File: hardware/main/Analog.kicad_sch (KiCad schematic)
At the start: 61 parts, among them J301 Overvoltage_protection, J302 Rad_sensor, J303 Mos_temp, J304 Diode_temp, U301 INA823DT, U302 INA823DT, U303 INA293A4, U304 INA293A4, U305 TL7726IDR_1

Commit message: Layout: Organize and initialize routing of control
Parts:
- added C315: 50V 100nF 0805, Capacitor_SMD:C_0805_2012Metric_Pad1.18x1.45mm_HandSolder, symbol Device:C_Small
- added D308: ESD351DPYR, Diode_SMD:D_0402_1005Metric_Pad0.77x0.64mm_HandSolder, symbol Device:D_TVS
- added R326: ?, Resistor_SMD:R_0805_2012Metric_Pad1.20x1.40mm_HandSolder, symbol Device:R_Small
- added TH303: NTC 10k 1SDNT2012X103F3950FTF, Resistor_SMD:R_0805_2012Metric_Pad1.20x1.40mm_HandSolder, symbol Device:Thermistor_NTC
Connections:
- net 3V3: now also R326.2
- net GNDA: now also C315.2, D308.1 (A1), TH303.2
- net I_panel_adc+: no longer D306.2 (A2)
- net V_bat_adc+: now also D306.2 (A2)
- new net V_temp_amb: C315.1, D308.2 (A2), R326.1, TH303.1
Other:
- moved on the sheet: C302, C303, J303, J304, R301, R302, TH301, TH302

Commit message: Schematics: Switch 2 Clamp inputs for better routing
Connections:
- net V_panel_adc+: now also U305.6 (D5); no longer U305.2 (D1)
- net V_temp_diode: now also U305.2 (D1); no longer U305.6 (D5)
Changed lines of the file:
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@@
     (stroke (width 0) (type default) (color 0 0 0 0))
   )
-  (label "V_panel_adc+" (at 179.07 45.72 0)
+  (label "V_panel_adc+" (at 222.885 53.34 0)
     (effects (font (size 1.016 1.016)) (justify left bottom))
   )
@@
     (effects (font (size 1.016 1.016)) (justify left bottom))
   )
-  (label "V_temp_diode" (at 222.885 53.34 0)
+  (label "V_temp_diode" (at 179.07 45.72 0)
     (effects (font (size 1.016 1.016)) (justify left bottom))
   )

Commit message: Layout: Designing thermal dissipation and optimizing control
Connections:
- net V_bat_adc+: now also U305.2 (D1); no longer U305.3 (D2)
- net V_panel_adc+: now also U305.7 (D6); no longer U305.6 (D5)
- net V_temp_diode: now also U305.6 (D5); no longer U305.2 (D1)
- net V_temp_mos: now also U305.3 (D2); no longer U305.7 (D6)
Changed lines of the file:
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@@
     (stroke (width 0) (type default) (color 0 0 0 0))
   )
-  (label "V_panel_adc+" (at 222.885 53.34 0)
+  (label "V_panel_adc+" (at 223.52 60.96 0)
     (effects (font (size 1.016 1.016)) (justify left bottom))
   )
@@
     (effects (font (size 1.016 1.016)) (justify left bottom))
   )
-  (label "V_temp_diode" (at 179.07 45.72 0)
+  (label "V_temp_diode" (at 222.885 53.34 0)
     (effects (font (size 1.016 1.016)) (justify left bottom))
   )
@@
     (effects (font (size 1.016 1.016)) (justify left bottom))
   )
-  (label "V_temp_mos" (at 223.52 60.96 0)
+  (label "V_temp_mos" (at 179.07 53.34 0)
     (effects (font (size 1.016 1.016)) (justify left bottom))
   )
@@
     (effects (font (size 1.016 1.016)) (justify left bottom))
   )
-  (label "V_bat_adc+" (at 179.07 53.34 0)
+  (label "V_bat_adc+" (at 179.07 45.72 0)
     (effects (font (size 1.016 1.016)) (justify left bottom))
   )

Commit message: Layout: Connect all unconected nets, and fix all DRC errors
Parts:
- JP301, JP302, JP303, JP304: footprint Zenite:SolderJumper-2_P0.5mm_Open_TrianglePad0.5x0.5mm -> Zenite:SolderJumper-2_P0.5mm_Open_TrianglePad0.8x0.5mm
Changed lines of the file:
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@@
     (property "Reference" "JP304" (id 0) (at 257.175 53.4502 0))
     (property "Value" "Disable_Ibat" (id 1) (at 257.175 55.9871 0))
-    (property "Footprint" "Zenite:SolderJumper-2_P0.5mm_Open_TrianglePad0.5x0.5mm" (id 2) (at 257.175 57.785 0)
+    (property "Footprint" "Zenite:SolderJumper-2_P0.5mm_Open_TrianglePad0.8x0.5mm" (id 2) (at 257.175 57.785 0)
       (effects (font (size 1.27 1.27)) hide)
     )
@@
     (property "Reference" "JP301" (id 0) (at 257.175 36.3052 0))
     (property "Value" "Disable_Vpanel" (id 1) (at 257.175 38.8421 0))
-    (property "Footprint" "Zenite:SolderJumper-2_P0.5mm_Open_TrianglePad0.5x0.5mm" (id 2) (at 257.175 40.64 0)
+    (property "Footprint" "Zenite:SolderJumper-2_P0.5mm_Open_TrianglePad0.8x0.5mm" (id 2) (at 257.175 40.64 0)
       (effects (font (size 1.27 1.27)) hide)
     )
@@
     (property "Reference" "JP302" (id 0) (at 257.175 42.0202 0))
     (property "Value" "Disable_Vbat" (id 1) (at 257.175 44.5571 0))
-    (property "Footprint" "Zenite:SolderJumper-2_P0.5mm_Open_TrianglePad0.5x0.5mm" (id 2) (at 257.175 46.355 0)
+    (property "Footprint" "Zenite:SolderJumper-2_P0.5mm_Open_TrianglePad0.8x0.5mm" (id 2) (at 257.175 46.355 0)
       (effects (font (size 1.27 1.27)) hide)
     )
@@
     (property "Reference" "JP303" (id 0) (at 257.175 47.7352 0))
     (property "Value" "Disabel_Ipanel" (id 1) (at 257.175 50.2721 0))
-    (property "Footprint" "Zenite:SolderJumper-2_P0.5mm_Open_TrianglePad0.5x0.5mm" (id 2) (at 257.175 52.07 0)
-      (effects (font (size 1.27 1.27)) hide)
-    )
+    (property "Footprint" "Zenite:SolderJumper-2_P0.5mm_Open_TrianglePad0.8x0.5mm" (id 2) (at 257.175 52.07 0)
+      (effects (font (size 1.27 1.27)) hide)
+    )

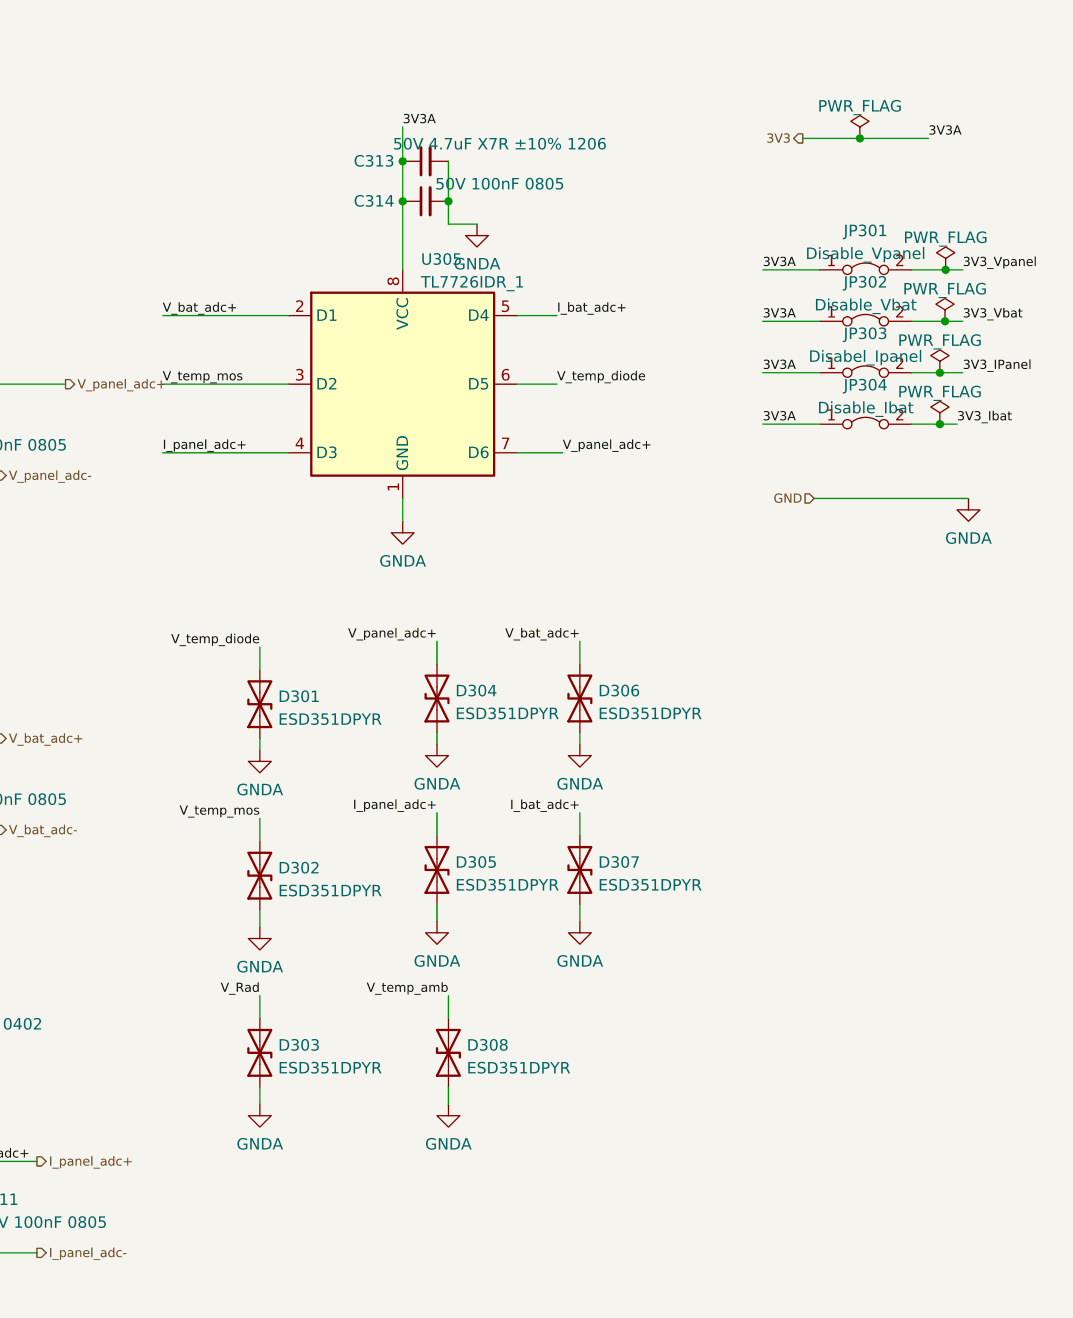
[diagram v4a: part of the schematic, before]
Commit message: layout: Separating analogical power nets
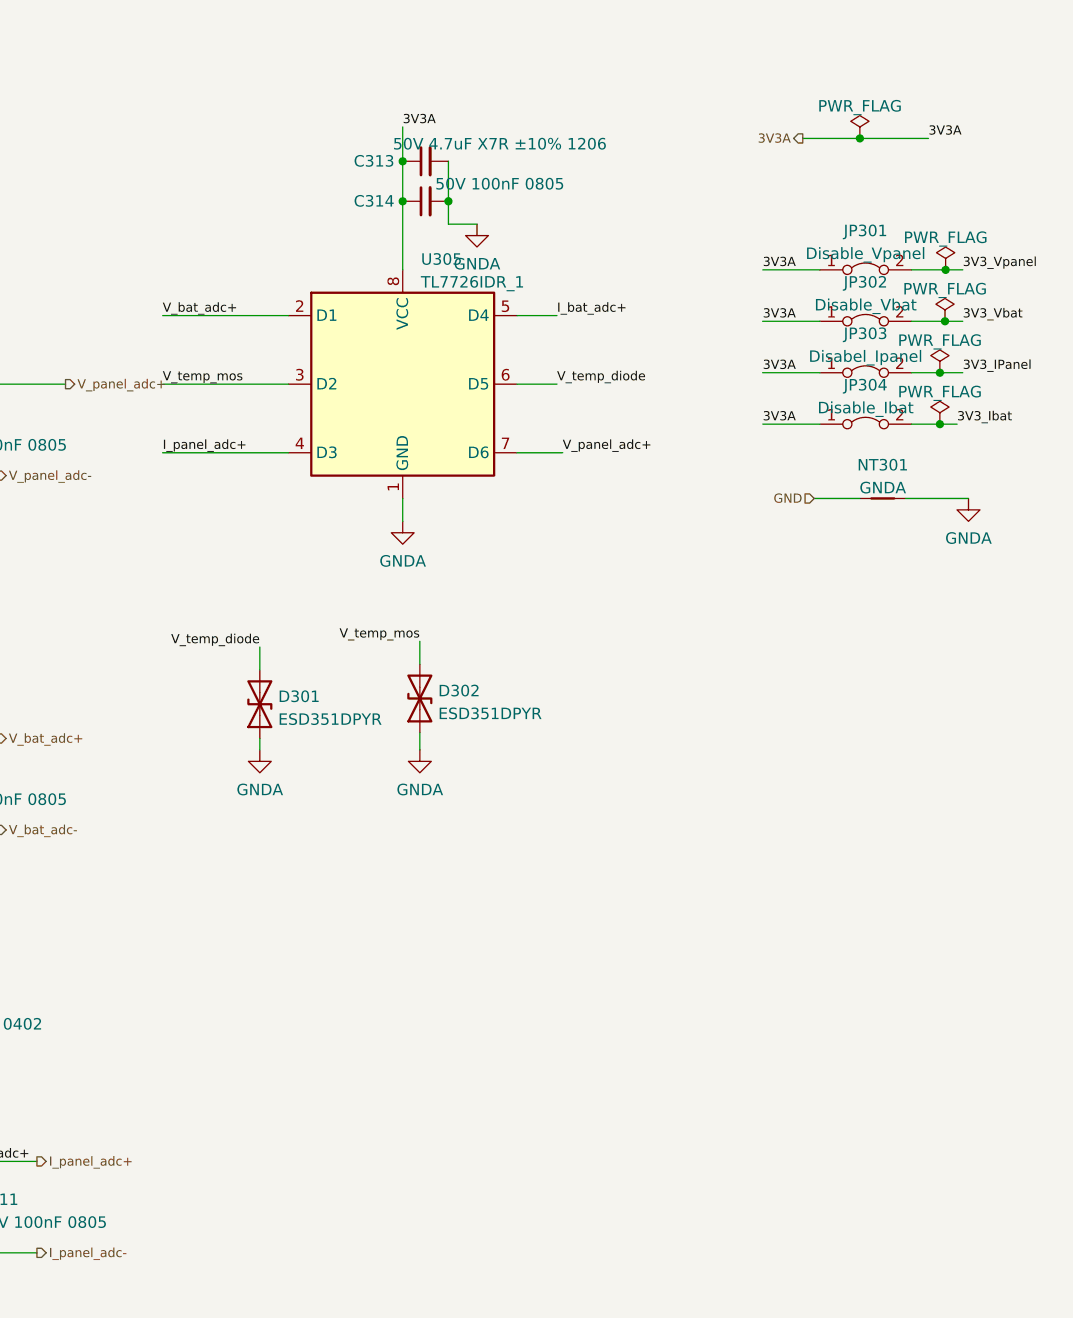
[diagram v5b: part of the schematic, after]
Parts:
- removed D303, D304, D305, D306, D307, D308: ESD351DPYR, Diode_SMD:D_0402_1005Metric_Pad0.77x0.64mm_HandSolder, symbol Device:D_TVS
- added NT301: GNDA, Resistor_SMD:R_0201_0603Metric, symbol Device:NetTie_2
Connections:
- net GNDA: now also NT301.2
- net 3V3 renamed 3V3A
- new net GND: NT301.1
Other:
- moved on the sheet: D302

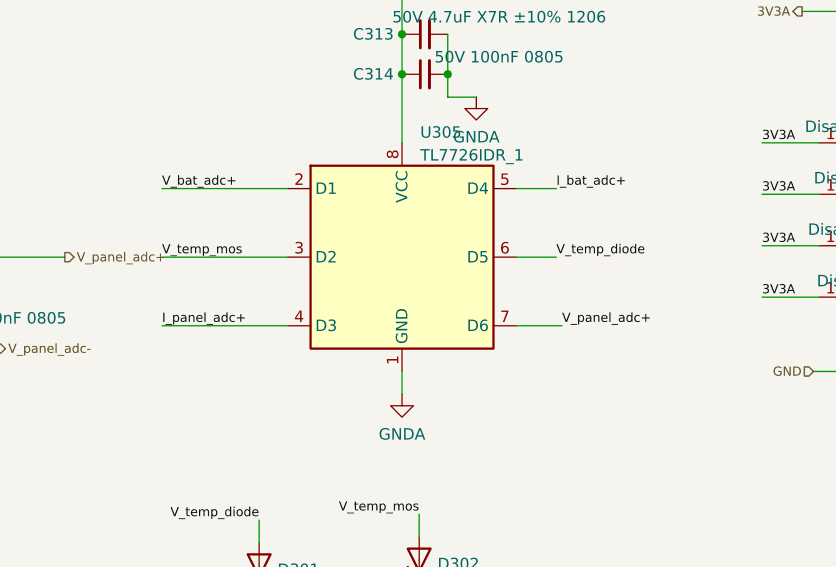
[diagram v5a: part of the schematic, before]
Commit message: Layout: Place components and route analog, supplies and CAN
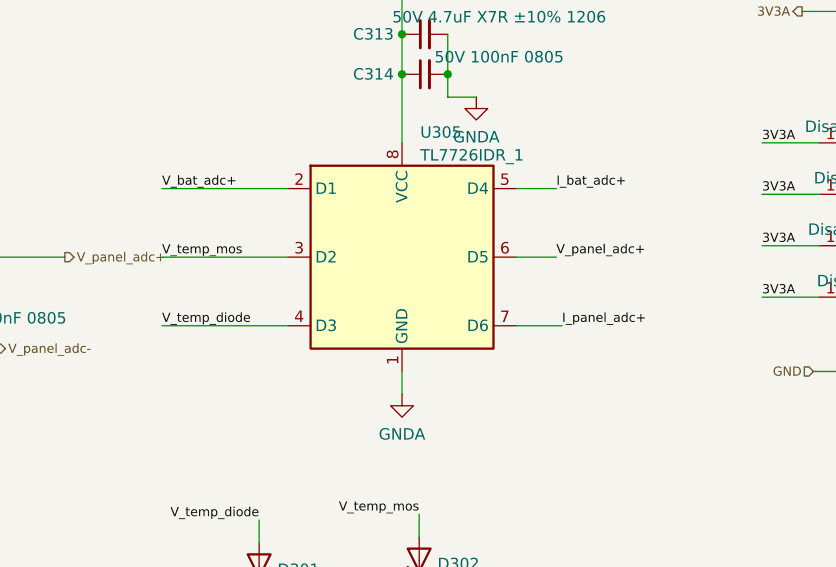
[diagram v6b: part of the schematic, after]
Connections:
- net I_panel_adc+: now also U305.7 (D6); no longer U305.4 (D3)
- net V_panel_adc+: now also U305.6 (D5); no longer U305.7 (D6)
- net V_temp_diode: now also U305.4 (D3); no longer U305.6 (D5)
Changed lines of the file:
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@@
     (stroke (width 0) (type default) (color 0 0 0 0))
   )
-  (label "V_panel_adc+" (at 223.52 60.96 0)
+  (label "V_panel_adc+" (at 222.885 53.34 0)
     (effects (font (size 1.016 1.016)) (justify left bottom))
   )
@@
     (effects (font (size 1.016 1.016)) (justify left bottom))
   )
-  (label "V_temp_diode" (at 222.885 53.34 0)
+  (label "V_temp_diode" (at 179.07 60.96 0)
     (effects (font (size 1.016 1.016)) (justify left bottom))
   )
@@
     (effects (font (size 1.016 1.016)) (justify left bottom))
   )
-  (label "I_panel_adc+" (at 179.07 60.96 0)
+  (label "I_panel_adc+" (at 223.52 60.96 0)
     (effects (font (size 1.016 1.016)) (justify left bottom))
   )
